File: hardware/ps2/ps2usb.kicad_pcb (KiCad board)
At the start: 2 copper layers, 60 x 39 mm, 19 parts, among them J1 DIN8, J2 DIN8, J3 USB1035, J4 Conn_01x03_Pin, U1 CH559L-less, Y1 12MHz

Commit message: Cleaned up rogue tracks.
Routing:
- net +5V: track 111.5 -> 109.4 mm
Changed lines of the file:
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@@
-	)
-	(segment
-		(start 129.55 116.2)
-		(end 129.55 116.075)
-		(width 0.25)
-		(layer "F.Cu")
-		(net 1)
 	)
 	(segment
@@
 		(net 1)
 	)
-	(segment
-		(start 129.55 116.075)
-		(end 129.5 116.025)
-		(width 0.25)
-		(layer "F.Cu")
-		(net 1)
-	)
 	(via
 		(at 129.55 116.2)
@@
 	)
 	(segment
-		(start 145.325 91.4)
-		(end 145.525 91.4)
-		(width 0.2032)
-		(layer "F.Cu")
-		(net 4)
-	)
-	(segment
 		(start 127.15 114.7)
 		(end 127.65 114.2)
@@
 	)
 	(segment
-		(start 145.325 90.6)
-		(end 145.2 90.6)
-		(width 0.254)
-		(layer "F.Cu")
-		(net 4)
-	)
-	(segment
-		(start 145.2 90.6)
-		(end 145.125 90.675)
-		(width 0.254)
-		(layer "F.Cu")
-		(net 4)
-	)
-	(segment
 		(start 150.225 94.815876)
 		(end 149.488524 94.0794)
@@
 	)
 	(segment
-		(start 117.275 97)
-		(end 115.58 97)
-		(width 0.889)
-		(layer "F.Cu")
-		(net 4)
-	)
-	(segment
 		(start 128.15 114.7)
 		(end 127.65 114.2)
@@
 	)
 	(segment
-		(start 143.525 92.2)
-		(end 143.596 92.129)
-		(width 0.2032)
-		(layer "F.Cu")
-		(net 6)
-	)
-	(segment
 		(start 132.6 98.700884)
 		(end 132.6 99)
@@
 	)
 	(segment
-		(start 143.4476 107.6024)
-		(end 143.525 107.525)
-		(width 0.25)
-		(layer "F.Cu")
-		(net 8)
-	)
-	(segment
 		(start 149.8726 104.4226)
 		(end 150.3226 104.8726)
@@
 		(net 8)
 	)
-	(segment
-		(start 143.525 107.525)
-		(end 143.7 107.525)
-		(width 0.25)
-		(layer "F.Cu")
-		(net 8)
-	)
 	(via
 		(at 126.975 104.225)
@@
 		(width 0.2032)
 		(layer "F.Cu")
-		(net 26)
-	)
-	(segment
-		(start 112.96 99.5)
-		(end 112.96 99.81)
-		(width 0.2032)
-		(layer "F.Cu")

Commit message: Clean up of labels and logo.
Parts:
- renumbered C6 to C5, C5 to C6

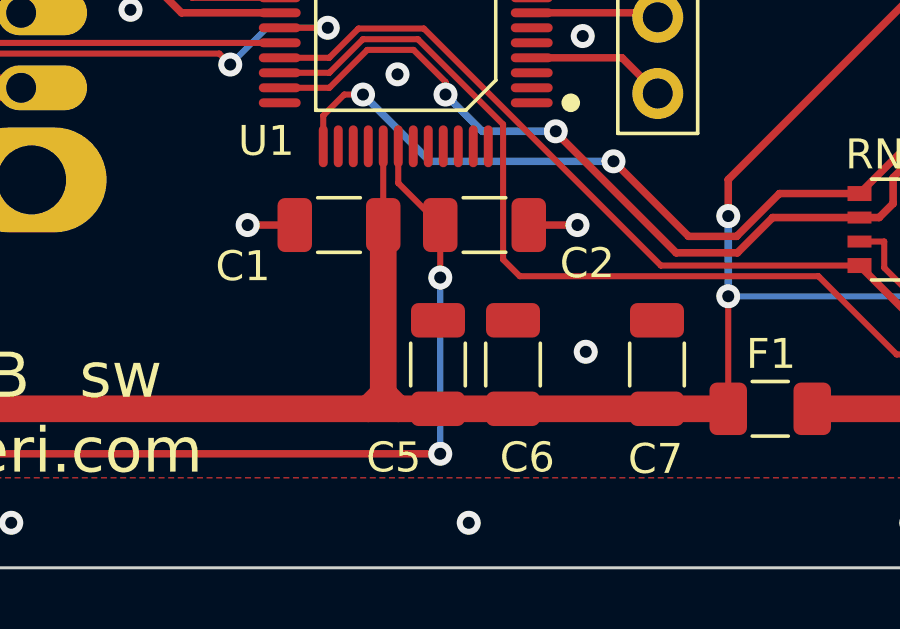
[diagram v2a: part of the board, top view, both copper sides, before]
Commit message: Corrected SMD sizes, updated BOM and placement.
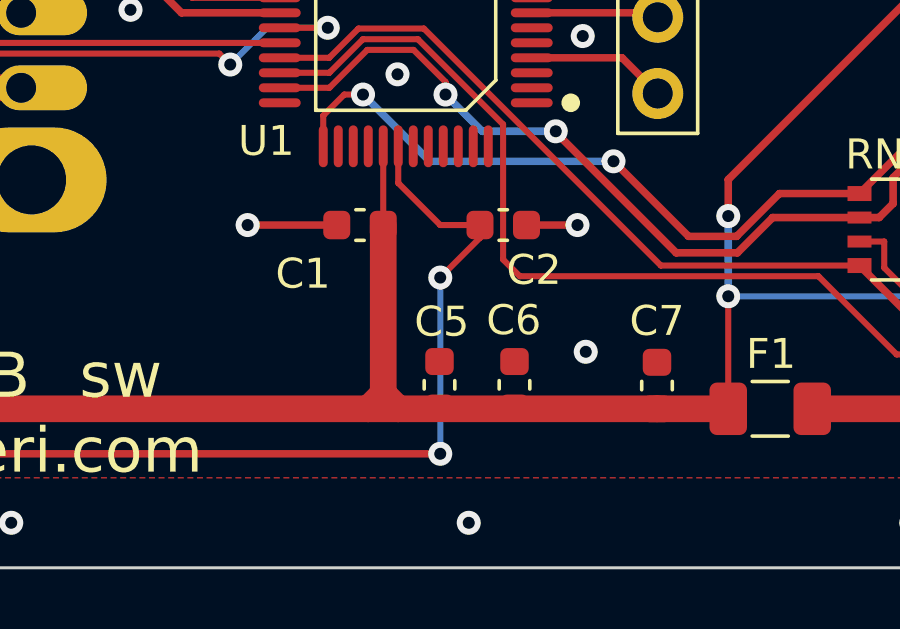
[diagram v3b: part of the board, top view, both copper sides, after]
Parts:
- C1, C2, C5, C6, C7: footprint Capacitor_SMD:C_1206_3216Metric -> Capacitor_SMD:C_0603_1608Metric
- moved C1 0.70 mm to (126.9, 108.6)
- moved C7 0.70 mm to (136.8, 113.9)
- moved C5 0.68 mm to (129.5, 113.9)
- moved C6 0.68 mm to (132.0, 113.9)
- moved C2 0.62 mm to (131.7, 108.6)
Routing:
- net +3.3V: track 44.2 -> 46.1 mm
- net GND: track 38.3 -> 39.7 mm
